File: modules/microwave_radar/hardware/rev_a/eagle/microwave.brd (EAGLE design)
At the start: 50 parts, among them J1 MODULE_GENERIC, J2 TC2030-JLINK-L, U1 SAM4LC8AA, U2 TLV62130, U3 MSGEQ7, U4 HB100, U5 OP284E_SEPARATE

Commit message: Finish adding attribute
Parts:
- removed C10, C9: 0.1uF, passives:0402_CAP
- removed C4: 1nF, passives:0402_CAP
- removed R12: 200k, passives:0402_RES
- added C23: 10uF, passives:0805_CAP
- added C24: 0.1uF, passives:0603_CAP
- added C25: 33pF, passives:0603_CAP
- added R16: 200k, passives:0603-RES
- C20: value 10uF -> 22uF; device passives:0402_CAP -> passives:0603_CAP
- C21: value 22uF -> 0.1uF; device passives:0402_CAP -> passives:0603_CAP
- C22: device passives:0402_CAP -> passives:1210_CAP
- C3: value 33pF -> 1nF; device passives:0402_CAP -> passives:0603_CAP
- moved C21 41.8 mm to (53.1, 4.32), turned to 0 degrees
- moved C3 11.2 mm to (38.6, 7.37), turned to 180 degrees
- moved C20 9.67 mm to (24.9, 32.3), turned to 270 degrees
- moved R11 8.03 mm to (29.0, 38.1)
- moved R15 5.59 mm to (29.0, 36.1)
- moved C22 2.54 mm to (30.5, 25.4)
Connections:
- net +3V3: now also C20.1, C21.2, R16.1; no longer C21.1, C9.2, R12.2
- net +5V: now also C23.P$1; no longer C20.1
- net AMP_OUT: now also C3.2; no longer C4.2
- net GND: now also C21.1, C23.P$2, C24.2, C25.2; no longer C10.2, C21.2, C3.1, C9.1
- net N$2: now also C25.1, R16.2; no longer C3.2, R12.1
- net N$3: now also C3.1; no longer C4.1
- net N$7: now also C24.1; no longer C10.1
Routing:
- net N$23: track 13.3 -> 2.83 mm
- net +3V3: track 268.4 -> 277.5 mm
- net N$24: track 18.2 -> 11.7 mm
- net N$20: track 2.54 -> 4.56 mm
- net N$1: track 20.5 -> 22.4 mm
- net +5V: track 88.0 -> 89.5 mm
- net N$7: track 14.6 -> 13.1 mm
- net AMP_OUT: track 71.4 -> 70.5 mm
- net GND: track 85.6 -> 84.9 mm, vias 19 -> 25
- net N$3: track 2.11 -> 2.72 mm

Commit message: Run Pat's script
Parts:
- removed C23: 10uF, passives:0805_CAP
- removed C25: 33pF, passives:0603_CAP
- added C4: 1nF, passives:0603_CAP
- added C9: 0.1uF, passives:0603_CAP
- C20: value 22uF -> 10uF; device passives:0603_CAP -> passives:0805_CAP
- C21: value 0.1uF -> 22uF
- C3: value 1nF -> 33pF
- moved C21 39.7 mm to (24.9, 32.3), turned to 270 degrees
- moved C20 13.6 mm to (22.9, 45.7), turned to 0 degrees
- moved C3 10.6 mm to (48.8, 4.32)
- renumbered C24 to C10, R16 to R12
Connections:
- net +3V3: now also C21.1, C9.2; no longer C20.1, C21.2
- net +5V: now also C20.P$1; no longer C23.P$1
- net AMP_OUT: now also C4.2; no longer C3.2
- net GND: now also C20.P$2, C21.2, C3.2, C9.1; no longer C20.2, C21.1, C23.P$2, C25.2
- net N$2: now also C3.1; no longer C25.1
- net N$3: now also C4.1; no longer C3.1
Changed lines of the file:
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@@
 </element>
 <element name="JP1" library="pinhead" package="1X06" value="" x="6.35" y="35.56" rot="R270"/>
-<element name="C23" library="passives" package="0805_CAP" value="10uF" x="22.86" y="45.72">
+<element name="C20" library="passives" package="0805_CAP" value="10uF" x="22.86" y="45.72">
 <attribute name="DIGIKEY" value="490-5523-1-ND" x="22.86" y="45.72" size="1.778" layer="27" display="off"/>
 </element>
-<element name="C20" library="passives" package="0603_CAP" value="22uF" x="24.892" y="32.258" rot="R270">
+<element name="C21" library="passives" package="0603_CAP" value="22uF" x="24.892" y="32.258" rot="R270">
 <attribute name="DIGIKEY" value="1276-1193-1-ND" x="24.892" y="32.258" size="1.778" layer="27" rot="R270" display="off"/>
 </element>
-<element name="C21" library="passives" package="0603_CAP" value="0.1uF" x="53.086" y="4.318">
+<element name="C9" library="passives" package="0603_CAP" value="0.1uF" x="53.086" y="4.318">
 <attribute name="DIGIKEY" value="490-1532-1-ND" x="53.086" y="4.318" size="1.778" layer="27" display="off"/>
 </element>
-<element name="C24" library="passives" package="0603_CAP" value="0.1uF" x="45.212" y="4.318">
+<element name="C10" library="passives" package="0603_CAP" value="0.1uF" x="45.212" y="4.318">
 <attribute name="DIGIKEY" value="490-1532-1-ND" x="45.212" y="4.318" size="1.778" layer="27" display="off"/>
 </element>
-<element name="C25" library="passives" package="0603_CAP" value="33pF" x="48.768" y="4.318" rot="R180">
+<element name="C3" library="passives" package="0603_CAP" value="33pF" x="48.768" y="4.318" rot="R180">
 <attribute name="DIGIKEY" value="490-1415-1-ND" x="48.768" y="4.318" size="1.778" layer="27" rot="R180" display="off"/>
 </element>
-<element name="C3" library="passives" package="0603_CAP" value="1nF" x="38.608" y="7.366" rot="R180">
+<element name="C4" library="passives" package="0603_CAP" value="1nF" x="38.608" y="7.366" rot="R180">
 <attribute name="DIGIKEY" value="490-1494-1-ND" x="38.608" y="7.366" size="1.778" layer="27" rot="R180" display="off"/>
 </element>
-<element name="R16" library="passives" package="0603-RES" value="200k" x="53.086" y="10.668" rot="R180">
+<element name="R12" library="passives" package="0603-RES" value="200k" x="53.086" y="10.668" rot="R180">
 <attribute name="DIGIKEY" value="RHM200KCFCT-ND" x="53.086" y="10.668" size="1.778" layer="27" rot="R180" display="off"/>
 </element>
@@
 <wire x1="10.668" y1="36.83" x2="11.938" y2="35.56" width="0.2032" layer="1"/>
 <wire x1="11.938" y1="35.56" x2="14.80693125" y2="35.56" width="0.2032" layer="1"/>
-<contactref element="C23" pad="P$2"/>
-<contactref element="C20" pad="2"/>
+<contactref element="C20" pad="P$2"/>
+<contactref element="C21" pad="2"/>
 <via x="25.4" y="40.64" extent="1-16" drill="0.2"/>
 <via x="24.892" y="41.148" extent="1-16" drill="0.2"/>
@@
 <wire x1="26.83" y1="40.89" x2="27.428" y2="40.89" width="0.2032" layer="1"/>
 <wire x1="27.428" y1="40.89" x2="27.94" y2="41.402" width="0.2032" layer="1"/>
-<contactref element="C21" pad="1"/>
-<contactref element="C25" pad="2"/>
-<contactref element="C24" pad="2"/>
+<contactref element="C9" pad="1"/>
+<contactref element="C3" pad="2"/>
+<contactref element="C10" pad="2"/>
 <wire x1="21.86" y1="45.72" x2="22.098" y2="45.958" width="0.4064" layer="1"/>
 <wire x1="22.098" y1="45.958" x2="22.098" y2="47.244" width="0.4064" layer="1"/>
@@
 <wire x1="37.084" y1="40.56506875" x2="37.084" y2="40.894" width="0.4064" layer="1"/>
 <wire x1="37.084" y1="40.894" x2="37.846" y2="41.656" width="0.4064" layer="1"/>
-<contactref element="C20" pad="1"/>
+<contactref element="C21" pad="1"/>
 <wire x1="29.38906875" y1="38.1" x2="29.21" y2="37.92093125" width="0.254" layer="1"/>
 <wire x1="29.21" y1="37.92093125" x2="29.21" y2="37.084" width="0.254" layer="1"/>
 <wire x1="29.21" y1="37.084" x2="28.52293125" y2="36.39693125" width="0.254" layer="1"/>
 <wire x1="28.52293125" y1="36.39693125" x2="28.52293125" y2="36.068" width="0.254" layer="1"/>
-<contactref element="C21" pad="2"/>
-<contactref element="R16" pad="1"/>
+<contactref element="C9" pad="2"/>
+<contactref element="R12" pad="1"/>
 <wire x1="53.736" y1="10.668" x2="53.736" y2="4.318" width="0.2032" layer="1"/>
 <wire x1="24.892" y1="32.908" x2="24.638" y2="33.162" width="0.4064" layer="1"/>
@@
 <wire x1="6.096" y1="45.72" x2="6.096" y2="42.164" width="0.2032" layer="1"/>
 <wire x1="6.096" y1="42.164" x2="6.35" y2="41.91" width="0.2032" layer="1"/>
-<contactref element="C23" pad="P$1"/>
+<contactref element="C20" pad="P$1"/>
 <wire x1="24.65" y1="42.07" x2="24.65" y2="43.18" width="0.4064" layer="1"/>
 <wire x1="24.65" y1="43.18" x2="24.65" y2="45.134" width="0.4064" layer="1"/>
@@
 <wire x1="10.16" y1="30.988" x2="10.16" y2="29.464" width="0.2032" layer="16"/>
 <wire x1="10.16" y1="29.464" x2="10.922" y2="28.702" width="0.2032" layer="16"/>
-<contactref element="C3" pad="2"/>
+<contactref element="C4" pad="2"/>
 <wire x1="35.814" y1="7.366" x2="37.958" y2="7.366" width="0.2032" layer="1"/>
 </signal>
@@
 <signal name="N$3">
 <contactref element="U3" pad="5"/>
-<contactref element="C3" pad="1"/>
+<contactref element="C4" pad="1"/>
 <wire x1="39.258" y1="7.366" x2="39.712" y2="7.62" width="0.2032" layer="1"/>
 <wire x1="39.712" y1="7.62" x2="41.91" y2="7.62" width="0.2032" layer="1"/>
@@
 <signal name="N$2">
 <contactref element="U3" pad="8"/>
-<contactref element="C25" pad="1"/>
+<contactref element="C3" pad="1"/>
 <wire x1="49.53" y1="7.62" x2="49.618" y2="7.532" width="0.2032" layer="1"/>
-<contactref element="R16" pad="2"/>
+<contactref element="R12" pad="2"/>
 <wire x1="49.53" y1="7.62" x2="51.562" y2="7.62" width="0.2032" layer="1"/>
 <wire x1="51.562" y1="7.62" x2="52.324" y2="8.382" width="0.2032" layer="1"/>
@@
 <contactref element="U3" pad="2"/>
 <wire x1="43.18" y1="11.43" x2="46.99" y2="15.24" width="0.2032" layer="1"/>
-<contactref element="C24" pad="1"/>
+<contactref element="C10" pad="1"/>
 <wire x1="43.18" y1="11.43" x2="43.18" y2="5.5" width="0.2032" layer="1"/>
 <wire x1="43.18" y1="5.5" x2="44.562" y2="4.318" width="0.2032" layer="1"/>

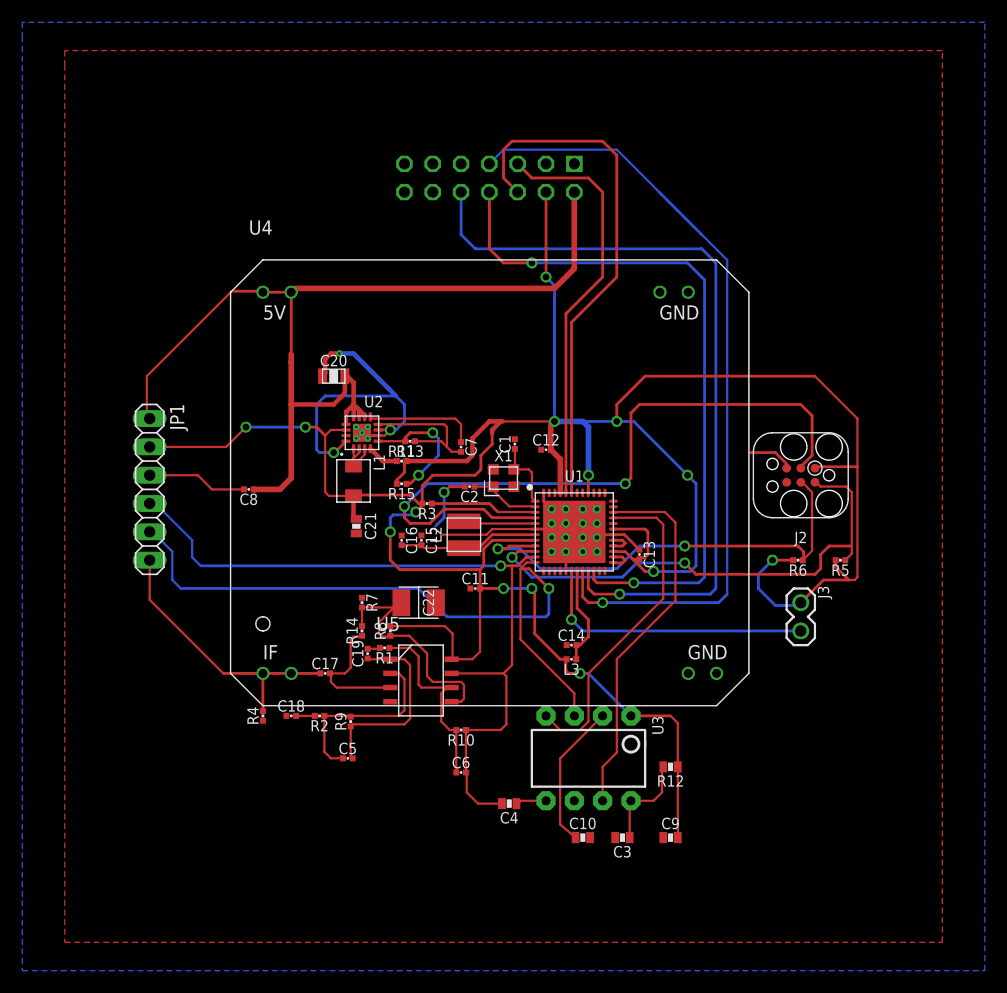
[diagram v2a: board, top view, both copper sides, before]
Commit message: Increase width of power trace
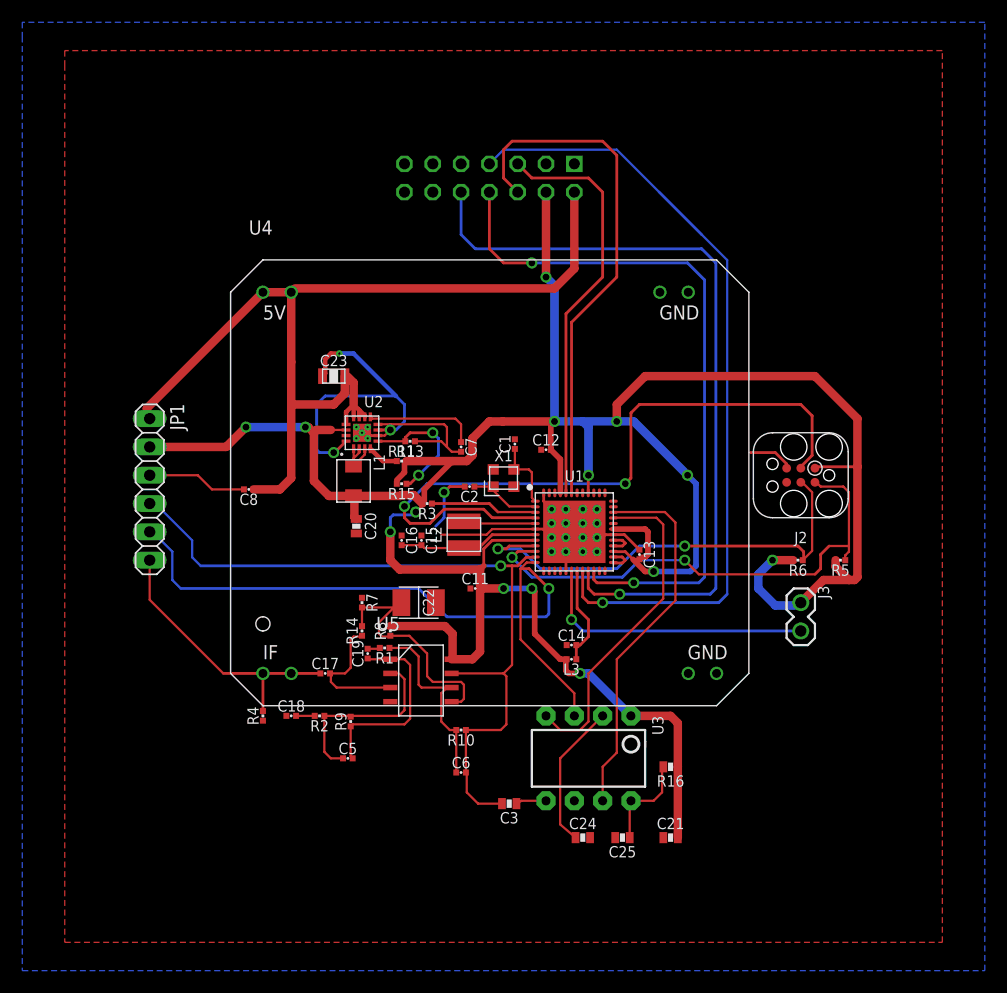
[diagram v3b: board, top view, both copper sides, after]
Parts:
- removed C4: 1nF, passives:0603_CAP
- removed C9: 0.1uF, passives:0603_CAP
- added C23: 10uF, passives:0805_CAP
- added C25: 33pF, passives:0603_CAP
- C20: value 10uF -> 22uF; device passives:0805_CAP -> passives:0603_CAP
- C21: value 22uF -> 0.1uF
- C3: value 33pF -> 1nF
- moved C21 39.7 mm to (53.1, 4.32), turned to 0 degrees
- moved C20 13.6 mm to (24.9, 32.3), turned to 270 degrees
- moved C3 10.6 mm to (38.6, 7.37)
- renumbered C10 to C24, R12 to R16
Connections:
- net +3V3: now also C20.1, C21.2; no longer C21.1, C9.2
- net +5V: now also C23.P$1; no longer C20.P$1
- net AMP_OUT: now also C3.2; no longer C4.2
- net GND: now also C20.2, C21.1, C23.P$2, C25.2; no longer C20.P$2, C21.2, C3.2, C9.1
- net N$2: now also C25.1; no longer C3.1
- net N$3: now also C3.1; no longer C4.1
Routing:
- net +3V3: track 277.5 -> 270.6 mm
- net +5V: track 89.5 -> 87.8 mm

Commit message: Add pin labels and logos
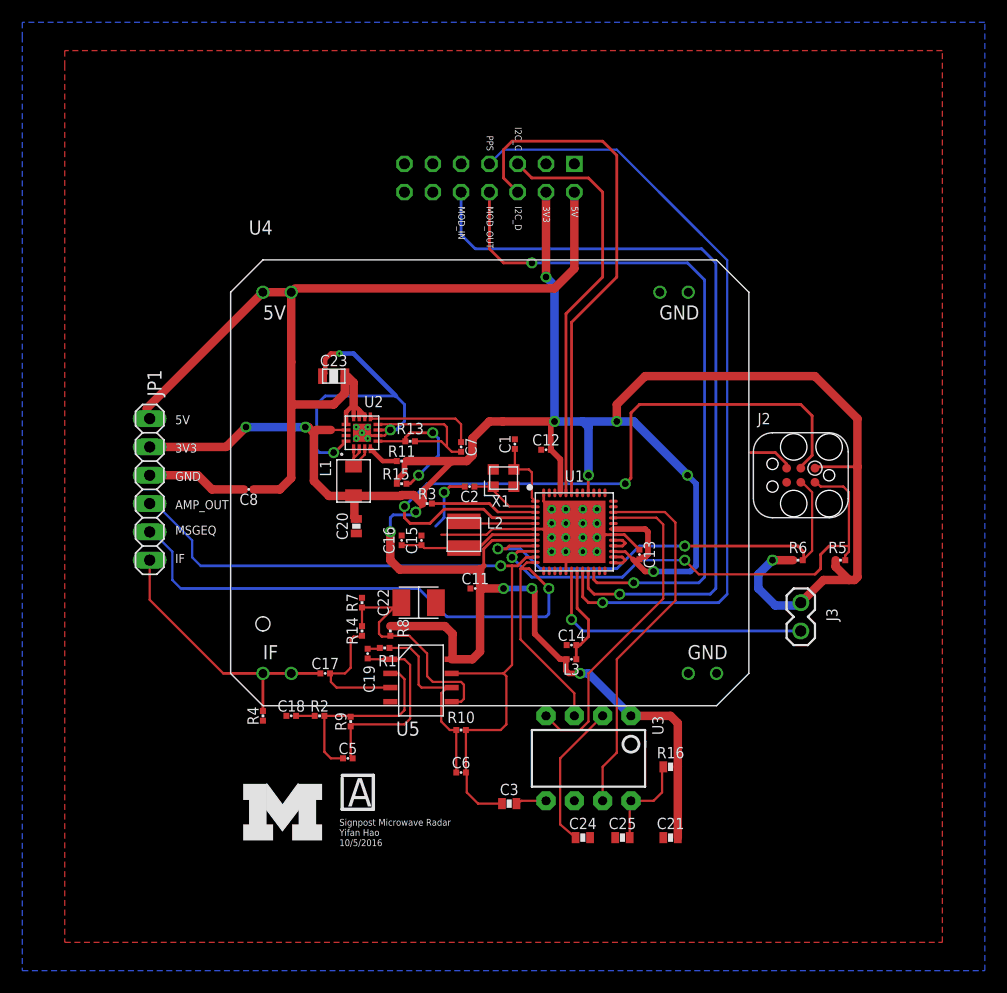
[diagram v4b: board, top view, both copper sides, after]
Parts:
- added U$1: (no value), logos:UMICH_SOLID_200MIL
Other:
- board text added: "3V3"
- board text added: "5V"
- board text added: "A"
- board text added: "AMP_OUT"
- board text added: "GND"
- board text added: "I2C_C"
- board text added: "I2C_D"
- board text added: "IF"
- board text added: "MOD_IN"
- board text added: "MOD_OUT"
- board text added: "MSGEQ"
- board text added: "PPS"
- board text added: "Signpost Microwave Radar Yifan Hao 10/5/2016"

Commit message: Add holes and add cap on HB100
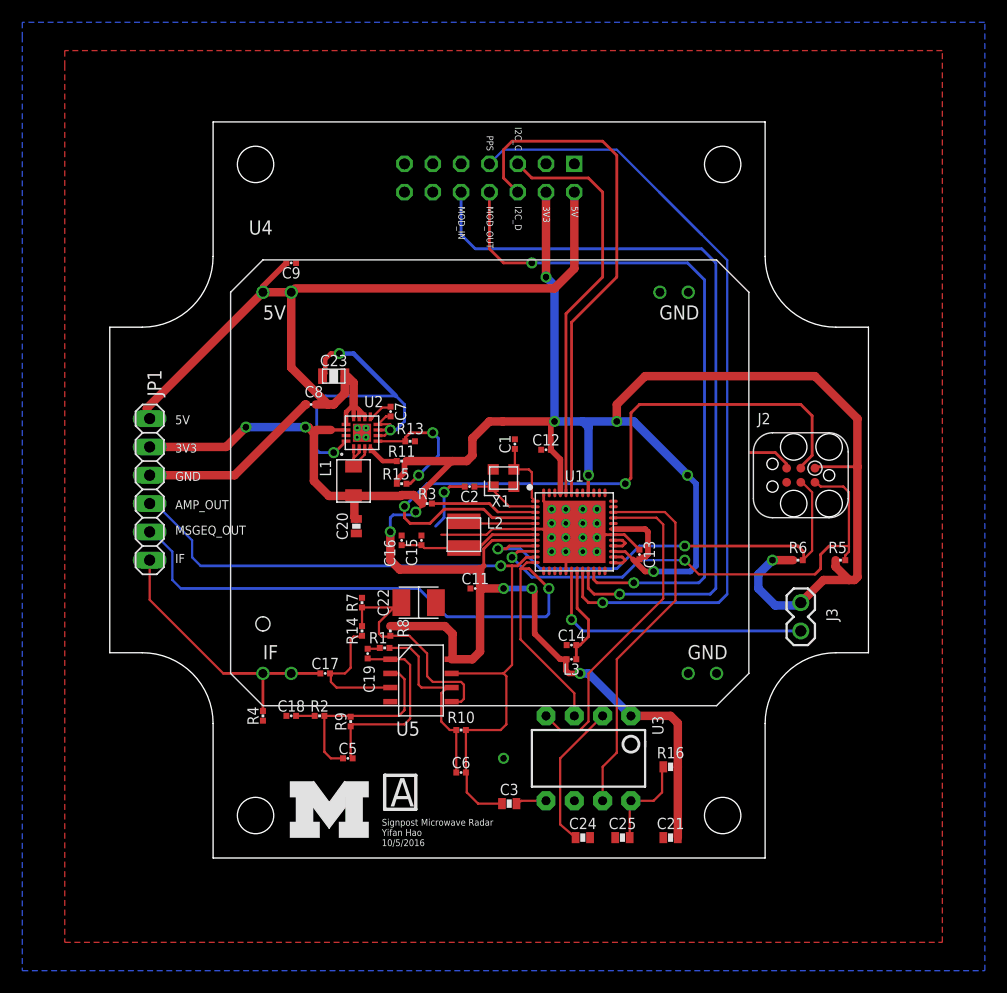
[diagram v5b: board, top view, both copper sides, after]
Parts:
- added C9: 100nF, passives:0402_CAP
- moved C8 9.45 mm to (20.8, 43.2)
- moved C7 7.08 mm to (28.0, 42.5)
- moved U$1 4.20 mm to (18.9, 4.29)
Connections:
- net +5V: now also C9.2
- net GND: now also C9.1
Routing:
- net +5V: track 87.8 -> 79.3 mm
- net N$8: track 10.0 -> 2.38 mm
- net GND: track 84.9 -> 81.0 mm
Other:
- board outline added: 68.1 x 66 mm
- board text added: "MSGEQ_OUT"
- board text removed: "MSGEQ"

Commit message: Run Pat's script after adding cap
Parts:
- removed C25: 33pF, passives:0603_CAP
- added C4: 1nF, passives:0603_CAP
- C17: value 4.7uF -> 100nF
- C20: value 22uF -> 4.7uF; device passives:0603_CAP -> passives:0402_CAP
- C21: value 0.1uF -> 10uF; device passives:0603_CAP -> passives:0805_CAP
- C22: value 100uF -> 22uF; device passives:1210_CAP -> passives:0603_CAP
- C23: value 10uF -> 100uF; device passives:0805_CAP -> passives:1210_CAP
- C3: value 1nF -> 33pF
- C9: value 100nF -> 0.1uF; device passives:0402_CAP -> passives:0603_CAP
- moved C9 61.8 mm to (53.1, 4.32), turned to 0 degrees
- moved C21 51.3 mm to (22.9, 45.7)
- moved C17 37.0 mm to (19.1, 55.9), turned to 180 degrees
- moved C23 21.7 mm to (30.5, 25.4), turned to 270 degrees
- moved C20 11.5 mm to (25.9, 20.8), turned to 90 degrees
- moved C3 10.6 mm to (48.8, 4.32)
- moved C22 8.85 mm to (24.9, 32.3)
- moved C19 8.85 mm to (19.1, 15.2), turned to 0 degrees
- moved C18 4.88 mm to (22.1, 19.1)
- renumbered C24 to C10, R16 to R12
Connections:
- net +3V3: now also C22.1, C9.2; no longer C20.1, C21.2
- net +5V: now also C17.2, C21.P$1; no longer C23.P$1, C9.2
- net AMP_OUT: now also C4.2; no longer C3.2
- net GND: now also C17.1, C19.1, C21.P$2, C22.2, C23.1, C3.2; no longer C18.1, C20.2, C21.1, C22.1, C23.P$2, C25.2
- net IF: now also C18.1; no longer C17.1
- net N$1: now also C23.2; no longer C22.2
- net N$15: now also C19.2; no longer C18.2
- net N$17: now also C20.1; no longer C19.1
- net N$18: now also C20.2; no longer C19.2
- net N$2: now also C3.1; no longer C25.1
- net N$3: now also C4.1; no longer C3.1
- net N$9: now also C18.2; no longer C17.2
